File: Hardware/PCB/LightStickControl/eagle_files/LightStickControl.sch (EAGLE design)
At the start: 3 parts

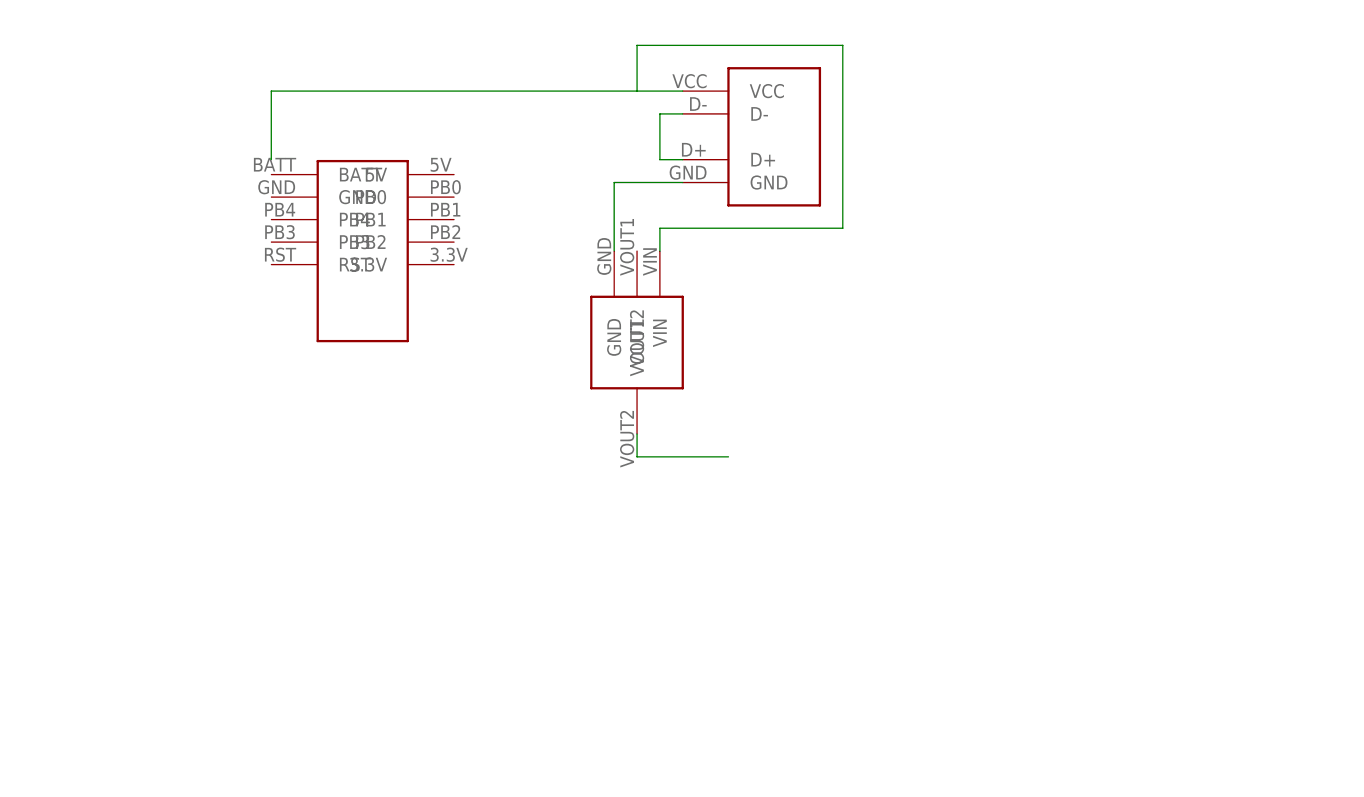
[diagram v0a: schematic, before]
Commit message: First cut of board layout. Add connectors. Label everything.
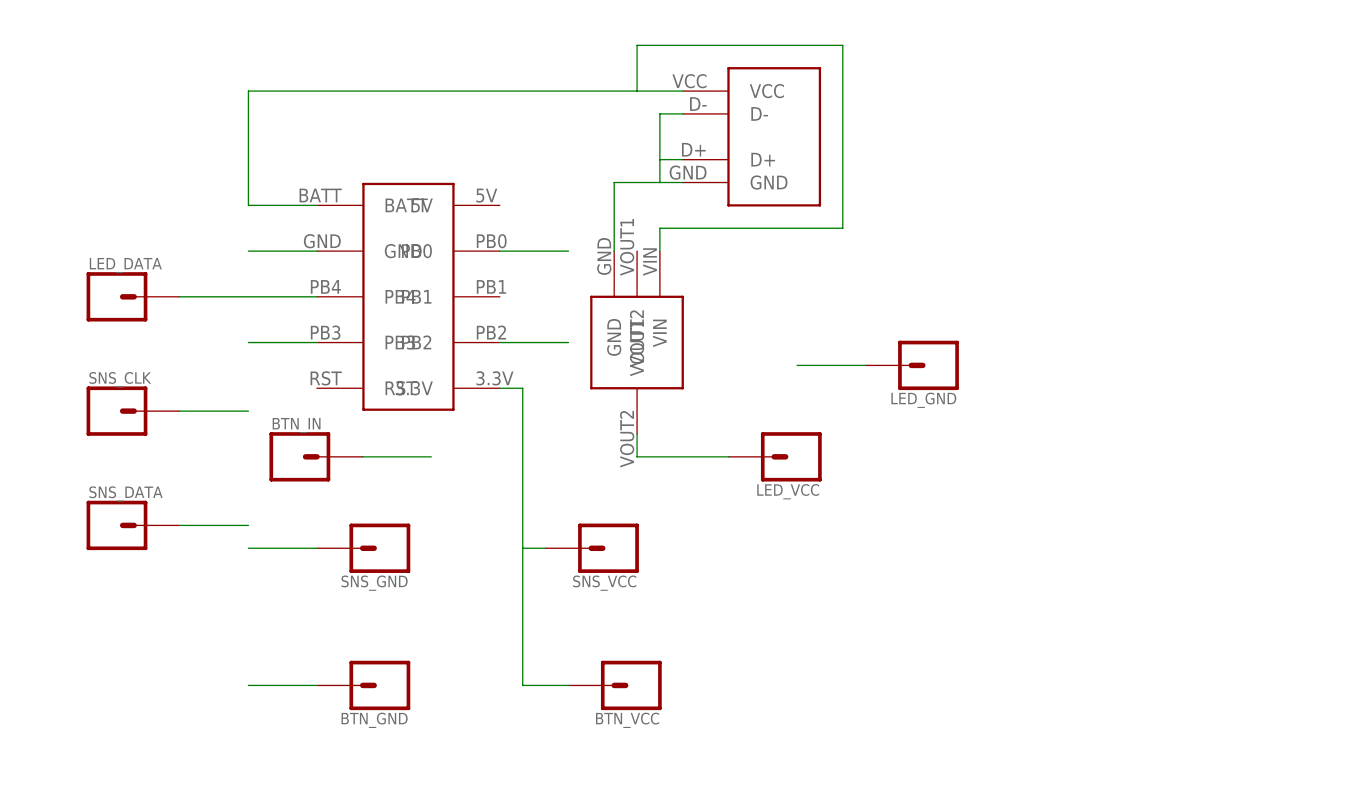
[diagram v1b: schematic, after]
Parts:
- added BTN_GND, BTN_IN, BTN_VCC, LED_DATA, LED_GND, LED_VCC, SNS_CLK, SNS_DATA, SNS_GND, SNS_VCC: (no value), SparkFun-Connectors:CONN_01
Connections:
- removed net N$1: USB1.GND, V1.GND
- removed net N$2: USB1.VCC, V1.VIN
- removed net N$3: V1.VOUT2
- removed net N$4: USB1.D+, USB1.D-
- new net BTN_IN: BTN_IN.1, MCU1.PB3
- new net GND: BTN_GND.1, LED_GND.1, MCU1.GND, SNS_GND.1, USB1.D+, USB1.D-, USB1.GND, V1.GND
- new net LED_DATA: LED_DATA.1, MCU1.PB4
- new net LED_VCC: LED_VCC.1, V1.VOUT2
- new net SNS_CLK: MCU1.PB2, SNS_CLK.1
- new net SNS_DATA: MCU1.PB0, SNS_DATA.1
- new net SNS_VCC: BTN_VCC.1, MCU1.3.3V, SNS_VCC.1
- new net VCC_IN: MCU1.BATT, USB1.VCC, V1.VIN

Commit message: Add support components and lay initial placement.
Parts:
- added C1, C2: 4.7uF, SparkFun-Capacitors:4.7UF0603
- added LED_DATA2, LED_GND2, LED_VCC2: (no value), SparkFun-Connectors:CONN_01
- renumbered LED_DATA to LED_DATA1, LED_GND to LED_GND1, LED_VCC to LED_VCC1
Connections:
- net GND: now also C1.2, C2.2, LED_GND2.1
- net LED_DATA: now also LED_DATA2.1
- net LED_VCC: now also C2.1, LED_VCC2.1
- net VCC_IN: now also C1.1
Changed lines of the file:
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@@
 <part name="USB1" library="freddyLibr" deviceset="USB_A_932" device=""/>
 <part name="MCU1" library="trinketLib" deviceset="ARDUINO_TRINKET" device=""/>
-<part name="LED_VCC" library="SparkFun-Connectors" deviceset="CONN_01" device=""/>
-<part name="LED_GND" library="SparkFun-Connectors" deviceset="CONN_01" device=""/>
+<part name="LED_VCC1" library="SparkFun-Connectors" deviceset="CONN_01" device=""/>
+<part name="LED_GND1" library="SparkFun-Connectors" deviceset="CONN_01" device=""/>
 <part name="SNS_VCC" library="SparkFun-Connectors" deviceset="CONN_01" device=""/>
 <part name="SNS_GND" library="SparkFun-Connectors" deviceset="CONN_01" device=""/>
-<part name="LED_DATA" library="SparkFun-Connectors" deviceset="CONN_01" device=""/>
+<part name="LED_DATA1" library="SparkFun-Connectors" deviceset="CONN_01" device=""/>
 <part name="SNS_CLK" library="SparkFun-Connectors" deviceset="CONN_01" device=""/>
 <part name="SNS_DATA" library="SparkFun-Connectors" deviceset="CONN_01" device=""/>
@@
 <part name="BTN_VCC" library="SparkFun-Connectors" deviceset="CONN_01" device=""/>
 <part name="BTN_GND" library="SparkFun-Connectors" deviceset="CONN_01" device=""/>
+<part name="C1" library="SparkFun-Capacitors" deviceset="4.7UF" device="0603" value="4.7uF"/>
+<part name="C2" library="SparkFun-Capacitors" deviceset="4.7UF" device="0603" value="4.7uF"/>
+<part name="LED_DATA2" library="SparkFun-Connectors" deviceset="CONN_01" device=""/>
+<part name="LED_VCC2" library="SparkFun-Connectors" deviceset="CONN_01" device=""/>
+<part name="LED_GND2" library="SparkFun-Connectors" deviceset="CONN_01" device=""/>
 </parts>
 <sheets>
@@
 <instance part="USB1" gate="G$1" x="68.58" y="53.34" rot="R270"/>
 <instance part="MCU1" gate="G$1" x="27.94" y="38.1"/>
-<instance part="LED_VCC" gate="G$1" x="71.12" y="17.78" smashed="yes" rot="R180">
+<instance part="LED_VCC1" gate="G$1" x="71.12" y="17.78" smashed="yes" rot="R180">
 <attribute name="VALUE" x="73.66" y="22.606" size="1.778" layer="96" font="vector" rot="R180"/>
 <attribute name="NAME" x="73.66" y="14.732" size="1.27" layer="95" font="vector" rot="R180"/>
 </instance>
-<instance part="LED_GND" gate="G$1" x="86.36" y="27.94" smashed="yes" rot="R180">
+<instance part="LED_GND1" gate="G$1" x="86.36" y="27.94" smashed="yes" rot="R180">
 <attribute name="VALUE" x="88.9" y="32.766" size="1.778" layer="96" font="vector" rot="R180"/>
 <attribute name="NAME" x="88.9" y="24.892" size="1.27" layer="95" font="vector" rot="R180"/>
@@
 <attribute name="NAME" x="27.94" y="4.572" size="1.27" layer="95" font="vector" rot="R180"/>
 </instance>
-<instance part="LED_DATA" gate="G$1" x="-5.08" y="35.56" smashed="yes">
+<instance part="LED_DATA1" gate="G$1" x="-5.08" y="35.56" smashed="yes">
 <attribute name="VALUE" x="-7.62" y="30.734" size="1.778" layer="96" font="vector"/>
 <attribute name="NAME" x="-7.62" y="38.608" size="1.27" layer="95" font="vector"/>
@@
 <attribute name="NAME" x="27.94" y="-10.668" size="1.27" layer="95" font="vector" rot="R180"/>
 </instance>
+<instance part="C1" gate="G$1" x="43.18" y="50.8"/>
+<instance part="C2" gate="G$1" x="60.96" y="25.4" rot="R180"/>
+<instance part="LED_DATA2" gate="G$1" x="-12.7" y="48.26" smashed="yes">
+<attribute name="VALUE" x="-15.24" y="43.434" size="1.778" layer="96" font="vector"/>
+<attribute name="NAME" x="-15.24" y="51.308" size="1.27" layer="95" font="vector"/>
+</instance>
+<instance part="LED_VCC2" gate="G$1" x="73.66" y="5.08" smashed="yes" rot="R180">
+<attribute name="VALUE" x="76.2" y="9.906" size="1.778" layer="96" font="vector" rot="R180"/>
+<attribute name="NAME" x="76.2" y="2.032" size="1.27" layer="95" font="vector" rot="R180"/>
+</instance>
+<instance part="LED_GND2" gate="G$1" x="88.9" y="38.1" smashed="yes" rot="R180">
+<attribute name="VALUE" x="91.44" y="42.926" size="1.778" layer="96" font="vector" rot="R180"/>
+<attribute name="NAME" x="91.44" y="35.052" size="1.27" layer="95" font="vector" rot="R180"/>
+</instance>
 </instances>
 <busses>
@@
 <pinref part="USB1" gate="G$1" pin="D-"/>
 <wire x1="55.88" y1="55.88" x2="58.42" y2="55.88" width="0.1524" layer="91"/>
+<pinref part="C1" gate="G$1" pin="2"/>
+<wire x1="50.8" y1="48.26" x2="43.18" y2="48.26" width="0.1524" layer="91"/>
 </segment>
 <segment>
-<pinref part="LED_GND" gate="G$1" pin="1"/>
-<wire x1="78.74" y1="27.94" x2="71.12" y2="27.94" width="0.1524" layer="91"/>
+<pinref part="LED_GND1" gate="G$1" pin="1"/>
+<pinref part="C2" gate="G$1" pin="2"/>
+<wire x1="60.96" y1="27.94" x2="71.12" y2="27.94" width="0.1524" layer="91"/>
+<pinref part="LED_GND2" gate="G$1" pin="1"/>
+<wire x1="71.12" y1="27.94" x2="78.74" y2="27.94" width="0.1524" layer="91"/>
+<wire x1="81.28" y1="38.1" x2="71.12" y2="38.1" width="0.1524" layer="91"/>
+<wire x1="71.12" y1="38.1" x2="71.12" y2="27.94" width="0.1524" layer="91"/>
 </segment>
 <segment>
@@
 <pinref part="V1" gate="G$1" pin="VIN"/>
 <wire x1="55.88" y1="43.18" x2="55.88" y2="40.64" width="0.1524" layer="91"/>
-<wire x1="53.34" y1="58.42" x2="10.16" y2="58.42" width="0.1524" layer="91"/>
+<wire x1="53.34" y1="58.42" x2="43.18" y2="58.42" width="0.1524" layer="91"/>
+<wire x1="43.18" y1="58.42" x2="10.16" y2="58.42" width="0.1524" layer="91"/>
 <wire x1="10.16" y1="58.42" x2="10.16" y2="45.72" width="0.1524" layer="91"/>
 <wire x1="10.16" y1="45.72" x2="17.78" y2="45.72" width="0.1524" layer="91"/>
 <pinref part="MCU1" gate="G$1" pin="BATT"/>
+<pinref part="C1" gate="G$1" pin="1"/>
+<wire x1="43.18" y1="55.88" x2="43.18" y2="58.42" width="0.1524" layer="91"/>
 </segment>
 </net>
@@
 <pinref part="V1" gate="G$1" pin="VOUT2"/>
 <wire x1="53.34" y1="20.32" x2="53.34" y2="17.78" width="0.1524" layer="91"/>
-<wire x1="53.34" y1="17.78" x2="63.5" y2="17.78" width="0.1524" layer="91"/>
-<pinref part="LED_VCC" gate="G$1" pin="1"/>
+<wire x1="53.34" y1="17.78" x2="60.96" y2="17.78" width="0.1524" layer="91"/>
+<pinref part="LED_VCC1" gate="G$1" pin="1"/>
+<pinref part="C2" gate="G$1" pin="1"/>
+<wire x1="60.96" y1="17.78" x2="63.5" y2="17.78" width="0.1524" layer="91"/>
+<wire x1="60.96" y1="20.32" x2="60.96" y2="17.78" width="0.1524" layer="91"/>
+<wire x1="60.96" y1="17.78" x2="60.96" y2="5.08" width="0.1524" layer="91"/>
+<pinref part="LED_VCC2" gate="G$1" pin="1"/>
+<wire x1="60.96" y1="5.08" x2="66.04" y2="5.08" width="0.1524" layer="91"/>
 </segment>
 </net>
 <net name="LED_DATA" class="0">
 <segment>
-<pinref part="LED_DATA" gate="G$1" pin="1"/>
+<pinref part="LED_DATA1" gate="G$1" pin="1"/>
 <pinref part="MCU1" gate="G$1" pin="PB4"/>
-<wire x1="2.54" y1="35.56" x2="17.78" y2="35.56" width="0.1524" layer="91"/>
+<wire x1="2.54" y1="35.56" x2="5.08" y2="35.56" width="0.1524" layer="91"/>
+<pinref part="LED_DATA2" gate="G$1" pin="1"/>
+<wire x1="5.08" y1="35.56" x2="17.78" y2="35.56" width="0.1524" layer="91"/>
+<wire x1="-5.08" y1="48.26" x2="5.08" y2="48.26" width="0.1524" layer="91"/>
+<wire x1="5.08" y1="48.26" x2="5.08" y2="35.56" width="0.1524" layer="91"/>
 </segment>
 </net>

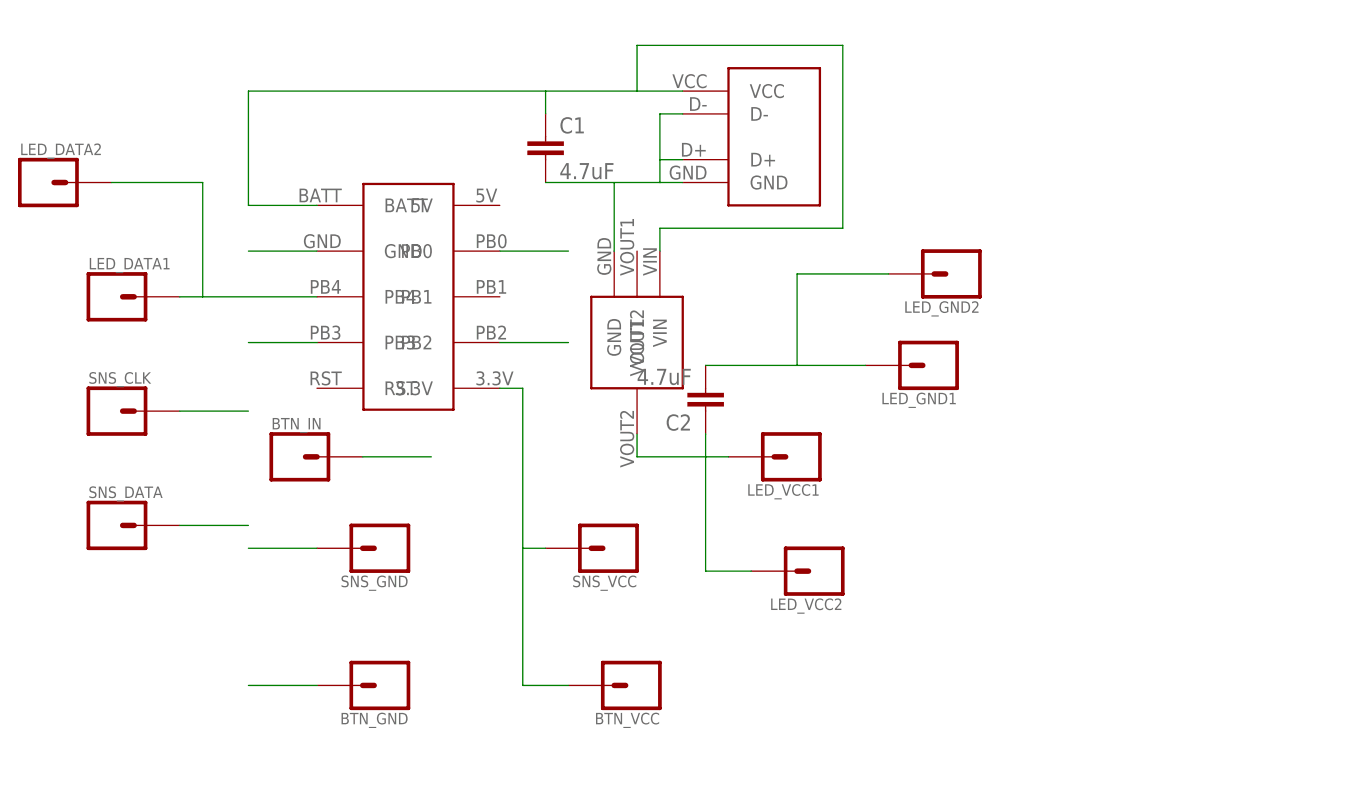
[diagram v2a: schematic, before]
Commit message: Add new switching voltage regulator.
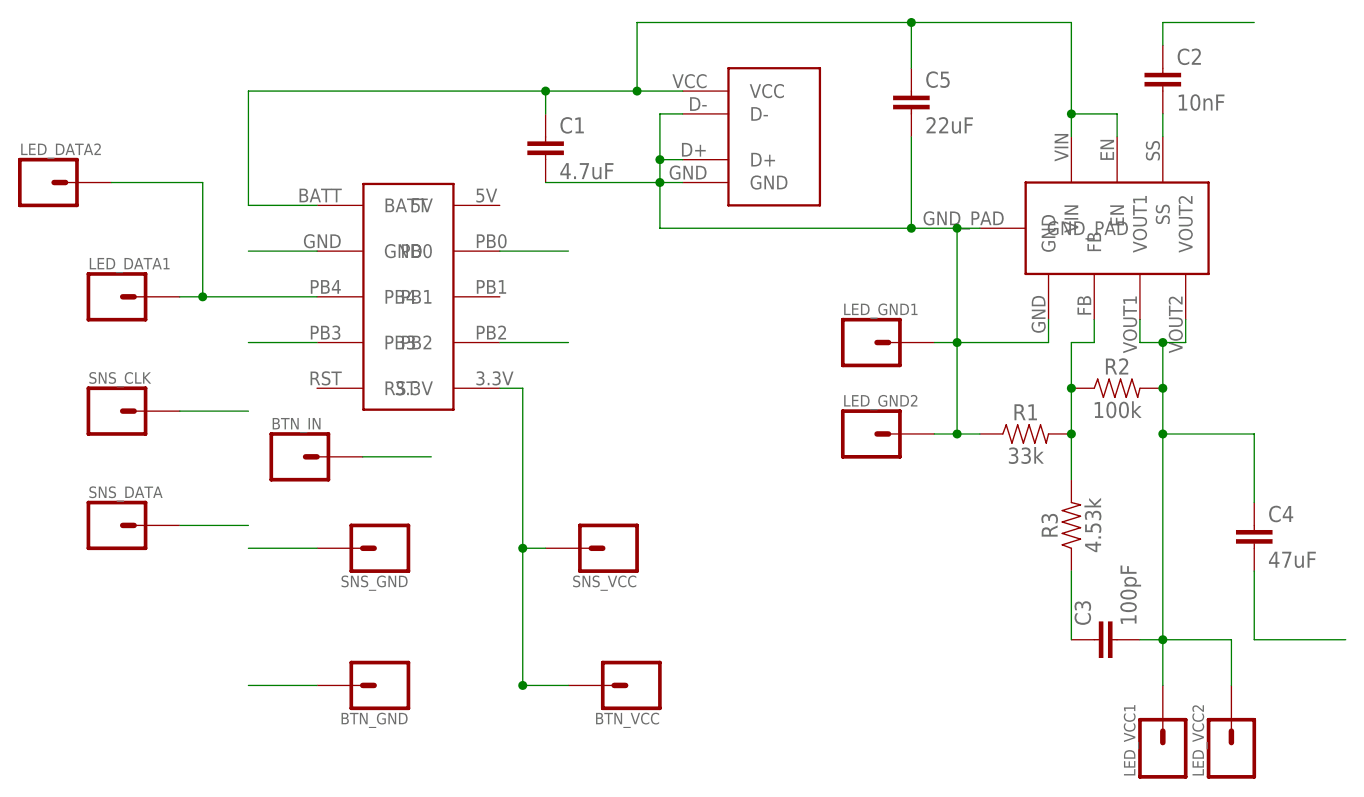
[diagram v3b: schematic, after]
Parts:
- added C3: 100pF, SparkFun-Capacitors:100PF-0603-50V-5%
- added C4: 47uF, SparkFun-Capacitors:22UF-0805-6.3V-20%
- added C5: 22uF, SparkFun-Capacitors:22UF-0805-6.3V-20%
- added R1: 33k, SparkFun-Resistors:33KOHM-0603-1/10W-1%
- added R2: 100k, SparkFun-Resistors:100KOHM-0603-1/10W-1%
- added R3: 4.53k, SparkFun-Resistors:4.7KOHM-0603-1/10W-1%
- C2: value 4.7uF -> 10nF; device SparkFun-Capacitors:4.7UF0603 -> SparkFun-Capacitors:10NF-0603-50V-10%
- V1: value VOLTAGE_REGULATOR_AP2114H -> LMZ10503; device freddyLibr:VOLTAGE_REGULATOR_AP2114H -> freddyLibr:LMZ10503
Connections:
- removed net LED_VCC: C2.1, LED_VCC1.1, LED_VCC2.1, V1.VOUT2
- new net FB: R1.2, R2.1, R3.2, V1.FB
- new net SS: C2.2, V1.SS
- new net VOUT: C3.2, C4.1, LED_VCC1.1, LED_VCC2.1, R2.2, V1.VOUT1, V1.VOUT2
- new net VOUT_C: C3.1, R3.1
- net GND: now also C2.1, C4.2, C5.2, R1.1, V1.GND_PAD; no longer C2.2
- net VCC_IN: now also C5.1, V1.EN
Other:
- moved on the sheet: C2, LED_GND1, LED_GND2, LED_VCC1, LED_VCC2
